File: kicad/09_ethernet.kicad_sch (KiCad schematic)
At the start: 0 parts

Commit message: Schematic complete: ethernet, emmc and adc sheets
- 09 ethernet: KSZ9031RNX with the Agilex 5 values and straps, RGMII 22R series,
  ferrite-fed analog rails, magjack J9, jack LED via 74LVC1G06
- 10 emmc: KIOXIA THGAMVG7T13BAIL, 47k pulls, CLK 10R, VCC 3V3 / VCCQ 1V8
- 13 adc: Agilex 3 card front end (SN74LV4051A, OPA365, 33R + 680p C0G,
  ADS7056 with DVDD 1V8), rail monitors on the mux
- attach/series_r/pull_r sheet helpers; STATUS.md updated

ERC: only the two known notes; all 92 pin-plan signals reach their loads.

Co-Authored-By: Claude Opus 5.5 <noreply@anthropic.com>
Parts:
- added C901, C921, C922, C924, C931, C932, C933, C934, C935, C936, C941, C942, C943, C950, C951: 100n, Capacitor_SMD:C_0402_1005Metric, symbol ti135_card:C
- added C910, C911: 27p, Capacitor_SMD:C_0402_1005Metric, symbol ti135_card:C
- added C920, C923: 22u, Capacitor_SMD:C_0805_2012Metric, symbol ti135_card:C
- added C930: 10u, Capacitor_SMD:C_0805_2012Metric, symbol ti135_card:C
- added C940: 4u7, Capacitor_SMD:C_0402_1005Metric, symbol ti135_card:C
- added FB901, FB902: BLM15PX121SN1D, Inductor_SMD:L_0402_1005Metric, symbol ti135_card:FerriteBead_Small
- added J9: RB1-125B8G1A, Connector_RJ:RJ45_UDE_RB1-125B8G1A, symbol ti135_card:RJ45_RB1-125B8G1A
- added R901, R902, R903, R904, R905, R906, R907, R908, R909, R910, R911, R912: 22R, Resistor_SMD:R_0402_1005Metric, symbol ti135_card:R
- added R920, R921, R922, R923, R924, R925, R926, R927: 4k7, Resistor_SMD:R_0402_1005Metric, symbol ti135_card:R
- added R928, R929: 1k, Resistor_SMD:R_0402_1005Metric, symbol ti135_card:R
- added R930: 10k, Resistor_SMD:R_0402_1005Metric, symbol ti135_card:R
- added R931: 12.1k 1%, Resistor_SMD:R_0402_1005Metric, symbol ti135_card:R
- added R950: 330R, Resistor_SMD:R_0402_1005Metric, symbol ti135_card:R
- added U901: KSZ9031RNXCA, Package_DFN_QFN:QFN-48-1EP_7x7mm_P0.5mm_EP5.15x5.15mm, symbol ti135_card:KSZ9031RNXCA
- added U902: 74LVC1G06GW, Package_TO_SOT_SMD:SOT-353_SC-70-5, symbol ti135_card:74LVC1G06
- added Y901: 25MHz, Crystal:Crystal_SMD_3225-4Pin_3.2x2.5mm, symbol ti135_card:Crystal_GND24
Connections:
- new net 1V2: C930.1, C931.1, C932.1, C933.1, C934.1, C935.1, C936.1, FB902.1, U901.14 (DVDDL), U901.18 (DVDDL), U901.23 (DVDDL), U901.26 (DVDDL), U901.30 (DVDDL), U901.39 (DVDDL), U901.4 (AVDDL), U901.9 (AVDDL)
- new net 1V8: C940.1, C941.1, C942.1, C943.1, C951.1, R920.1, R921.1, R922.1, R923.1, R924.1, R925.1, R926.1, R927.1, U901.16 (DVDDH), U901.34 (DVDDH), U901.40 (DVDDH), U902.5 (VCC)
- new net 3V3: FB901.1, R950.1
- new net GND: C901.2, C910.2, C911.2, C920.2, C921.2, C922.2, C923.2, C924.2, C930.2, C931.2, C932.2, C933.2, C934.2, C935.2, C936.2, C940.2, C941.2, C942.2, C943.2, C950.2, C951.2, J9.R10 (GND), J9.SH, R928.2, R929.2, R930.2, R931.2, U901.29 (VSS), U901.49 (PAD_GND), U902.3 (GND), Y901.2 (G), Y901.4 (G)
- new net eth_ct: C950.1, J9.R1 (CT)
- new net eth_int_n: R927.2, U901.38 (INT_N/PME_N2)
- new net eth_led_a: J9.L3, R950.2
- new net eth_led_k: J9.L4, U902.4
- new net eth_mdc: R926.2, U901.36 (MDC)
- new net eth_mdi_a_N: J9.R3 (TD1-), U901.3 (TXRXM_A)
- new net eth_mdi_a_P: J9.R2 (TD1+), U901.2 (TXRXP_A)
- new net eth_mdi_b_N: J9.R5 (TD2-), U901.6 (TXRXM_B)
- new net eth_mdi_b_P: J9.R4 (TD2+), U901.5 (TXRXP_B)
- new net eth_mdi_c_N: J9.R7 (TD3-), U901.8 (TXRXM_C)
- new net eth_mdi_c_P: J9.R6 (TD3+), U901.7 (TXRXP_C)
- new net eth_mdi_d_N: J9.R9 (TD4-), U901.11 (TXRXM_D)
- new net eth_mdi_d_P: J9.R8 (TD4+), U901.10 (TXRXP_D)
- new net eth_mdio: R925.2, U901.37 (MDIO)
- new net eth_rst_n: C901.1, R930.1, U901.42 (RESET_N)
- new net phy_avddh: C920.1, C921.1, C922.1, FB901.2, U901.1 (AVDDH), U901.12 (AVDDH)
- new net phy_avddl_pll: C923.1, C924.1, FB902.2, U901.44 (AVDDL_PLL)
- new net phy_iset: R931.1, U901.48 (ISET)
- new net phy_led1: R929.1, U901.17 (LED1/PHAD0/PME_N1), U902.2
- new net phy_led2: R928.1, U901.15 (LED2/PHYAD1)
- new net phy_led_mode: R924.2, U901.41 (CLK125_NDO/LED_MODE)
- new net phy_rx_ctl: R908.2, U901.33 (RX_DV/CLK125_EN)
- new net phy_rxc: R907.2, U901.35 (RX_CLK/PHYAD2)
- new net phy_rxd0: R909.2, U901.32 (RXD0/MODE0)
- new net phy_rxd1: R910.2, U901.31 (RXD1/MODE1)
- new net phy_rxd2: R911.2, U901.28 (RXD2/MODE2)
- new net phy_rxd3: R912.2, U901.27 (RXD3/MODE3)
- new net phy_tx_ctl: R902.2, U901.25 (TX_EN)
- new net phy_txc: R901.2, U901.24 (GTX_CLK)
- new net phy_txd0: R903.2, U901.19 (TXD0)
- new net phy_txd1: R904.2, U901.20 (TXD1)
- new net phy_txd2: R905.2, U901.21 (TXD2)
- new net phy_txd3: R906.2, U901.22 (TXD3)
- new net phy_xi: C910.1, U901.46 (XI), Y901.1
- new net phy_xo: C911.1, U901.45 (XO), Y901.3
- new net rgmii_rx_ctl: R908.1
- new net rgmii_rxc: R907.1
- new net rgmii_rxd0: R909.1, R920.2
- new net rgmii_rxd1: R910.1, R921.2
- new net rgmii_rxd2: R911.1, R922.2
- new net rgmii_rxd3: R912.1, R923.2
- new net rgmii_tx_ctl: R902.1
- new net rgmii_txc: R901.1
- new net rgmii_txd0: R903.1
- new net rgmii_txd1: R904.1
- new net rgmii_txd2: R905.1
- new net rgmii_txd3: R906.1
- no-connect marks 0 -> 5
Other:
- note added: "1V2 DVDDL/AVDDL (8 pins): 10u + 6 x 100n"
- note added: "1V8 DVDDH (3 pins): 4u7 + 3 x 100n"
- note added: "25 MHz crystal 3225, 27 p load (Agilex card values); place at the PHY"
- note added: "AVDDH (3V3) and AVDDL_PLL (1V2) through ferrites (Agilex FB1/FB2)"
- note added: "Jack LED: LED1 (1.8 V, active high with its PHYAD0 pull-down) -> U902 open-drain inverter -> LED cathode; anode via R950 to 3V3. Verify LED1 polarity at bring-up."
- note added: "KSZ9031RNX gigabit PHY, RGMII at 1.8 V to bank 4B. Values and straps from the Agilex 5 card (address 0, RGMII mode, single-LED mode). J9 = UDE RB1-125B8G1A magjack, placed per MECHANICAL.md."
- note added: "RGMII series 22 R: TX at the FPGA, RX at the PHY (source side)"
- note added: "Straps / pulls (1V8): MODE0..3 = 1 (RGMII), LED_MODE = 1 (single LED), PHYAD = 0, MDIO/MDC/INT pull-ups, RESET_N pull-down (PHY held in reset until the FPGA drives it)."

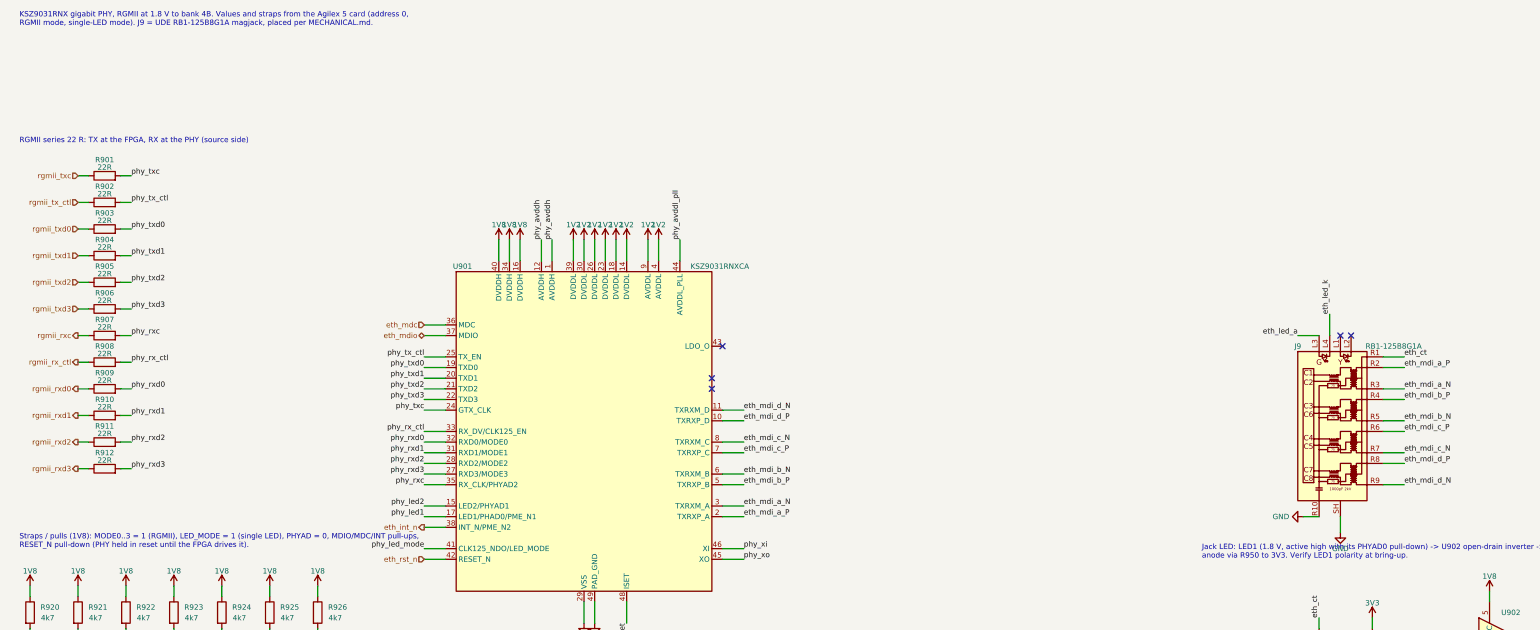
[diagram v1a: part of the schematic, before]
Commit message: PCB setup: board outline, fixed connectors, stack-up and rules; HR911130A magjack
- J9 magjack changed to HanRun HR911130A (C54408, 9124 orderable; RB1 had 0):
  generated footprint from the HanRun drawing, symbol, ethernet sheet updated,
  placed with the Ti60 jack's front face and centreline (MECHANICAL.md)
- tools/make_board.py: board from the netlist, outline, aux origin = Ti60
  origin, J3/J6 bottom sockets and J9 checked against MECHANICAL.md pads,
  U501 rotated 180 deg, U801 north, rest staged by sheet
- tools/board_setup.py: Agilex JLC08161H-3313 stack-up, LPDDR4/RGMII/power
  net classes, DRC rules (U501/U801), J3 edge exception
- DRC: parity 0, no shorts; only unrouted nets and edge silk warnings

Co-Authored-By: Claude Opus 5.5 <noreply@anthropic.com>
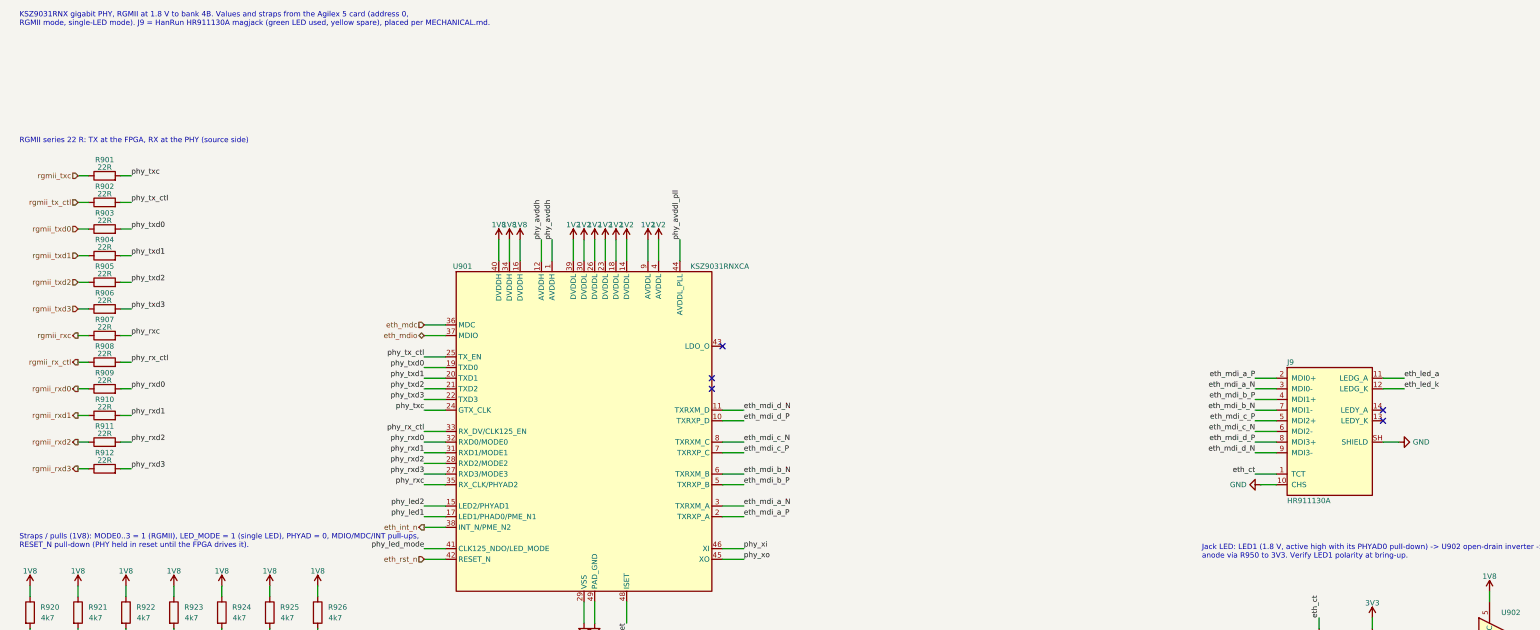
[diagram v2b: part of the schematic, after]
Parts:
- J9: value RB1-125B8G1A -> HR911130A; footprint Connector_RJ:RJ45_UDE_RB1-125B8G1A -> ti135_card:RJ45_Hanrun_HR911130A_Horizontal; symbol ti135_card:RJ45_RB1-125B8G1A -> ti135_card:HR911130A; LCSC C363353 -> C54408
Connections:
- net GND: now also J9.10 (CHS); no longer J9.R10 (GND)
- net eth_ct: now also J9.1 (TCT); no longer J9.R1 (CT)
- net eth_led_a: now also J9.11 (LEDG_A); no longer J9.L3
- net eth_led_k: now also J9.12 (LEDG_K); no longer J9.L4
- net eth_mdi_a_N: now also J9.3 (MDI0-); no longer J9.R3 (TD1-)
- net eth_mdi_a_P: now also J9.2 (MDI0+); no longer J9.R2 (TD1+)
- net eth_mdi_b_N: now also J9.7 (MDI1-); no longer J9.R5 (TD2-)
- net eth_mdi_b_P: now also J9.4 (MDI1+); no longer J9.R4 (TD2+)
- net eth_mdi_c_N: now also J9.6 (MDI2-); no longer J9.R7 (TD3-)
- net eth_mdi_c_P: now also J9.5 (MDI2+); no longer J9.R6 (TD3+)
- net eth_mdi_d_N: now also J9.9 (MDI3-); no longer J9.R9 (TD4-)
- net eth_mdi_d_P: now also J9.8 (MDI3+); no longer J9.R8 (TD4+)
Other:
- note added: "KSZ9031RNX gigabit PHY, RGMII at 1.8 V to bank 4B. Values and straps from the Agilex 5 card (address 0, RGMII mode, single-LED mode). J9 = HanRun HR911130A magjack (green LED used, yellow spare), placed per MECHANICAL.md."
- note removed: "KSZ9031RNX gigabit PHY, RGMII at 1.8 V to bank 4B. Values and straps from the Agilex 5 card (address 0, RGMII mode, single-LED mode). J9 = UDE RB1-125B8G1A magjack, placed per MECHANICAL.md."
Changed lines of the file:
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@@
 		(comment 1 "Efinix Ti135N484I3 control card for the AC lab PSU baseboard")
 	)
-	(text "KSZ9031RNX gigabit PHY, RGMII at 1.8 V to bank 4B. Values and straps from the Agilex 5 card (address 0,\nRGMII mode, single-LED mode). J9 = UDE RB1-125B8G1A magjack, placed per MECHANICAL.md."
+	(text "KSZ9031RNX gigabit PHY, RGMII at 1.8 V to bank 4B. Values and straps from the Agilex 5 card (address 0,\nRGMII mode, single-LED mode). J9 = HanRun HR911130A magjack (green LED used, yellow spare), placed per MECHANICAL.md."
 		(exclude_from_sim no)
 		(at 17.78 17.78 0)
@@
 	)
 	(symbol
-		(lib_id "ti135_card:RJ45_RB1-125B8G1A")
+		(lib_id "ti135_card:HR911130A")
 		(at 330.2 114.3 0)
 		(unit 1)
@@
 		(dnp no)
 		(property "Reference" "J9"
-			(at 322.58 93.98 0)
+			(at 320.04 97.79 0)
 			(effects
 				(font
 					(size 1.27 1.27)
 				)
+				(justify left)
 			)
 		)
-		(property "Value" "RB1-125B8G1A"
-			(at 345.44 93.98 0)
+		(property "Value" "HR911130A"
+			(at 320.04 130.81 0)
 			(effects
 				(font
 					(size 1.27 1.27)
 				)
+				(justify left)
 			)
 		)
-		(property "Footprint" "Connector_RJ:RJ45_UDE_RB1-125B8G1A"
-			(at 331.47 111.76 0)
+		(property "Footprint" "ti135_card:RJ45_Hanrun_HR911130A_Horizontal"
+			(at 330.2 114.3 0)
 			(effects
 				(font
@@
 			)
 		)
-		(property "Datasheet" ""
-			(at 324.104 113.157 0)
+		(property "Datasheet" "https://datasheet.lcsc.com/datasheet/pdf/d9b1e130e54a44fe9872ced55aa393e4.pdf"
+			(at 330.2 114.3 0)
 			(effects
 				(font
 					(size 1.27 1.27)
 				)
-				(justify left top)
 				(hide yes)
 			)
 		)
-		(property "Description" "LAN Transformer Jack, RJ45, 10/100/1000 BaseT"
+		(property "Description" "HanRun RJ45 with 10/100/1000Base-T magnetics, green (11 A / 12 K) and yellow (14 A / 13 K) LEDs. TCT = chip-side centre taps, CHS = 75 R / 1000 p Bob Smith common (LCSC C54408)"
 			(at 330.2 114.3 0)
 			(effects
@@
 			)
 		)
-		(property "LCSC" "C363353"
+		(property "LCSC" "C54408"
 			(at 330.2 114.3 0)
 			(effects
@@
 			)
 		)
-		(pin "R10"
+		(pin "2"
 		)
-		(pin "L1"
+		(pin "3"
 		)
-		(pin "L2"
+		(pin "4"
 		)
-		(pin "L3"
+		(pin "7"
 		)
-		(pin "L4"
+		(pin "5"
 		)
-		(pin "R1"
+		(pin "6"
 		)
-		(pin "R2"
+		(pin "8"
 		)
-		(pin "R3"
+		(pin "9"
 		)
-		(pin "R4"
+		(pin "1"
 		)
-		(pin "R5"
+		(pin "10"
 		)
-		(pin "R6"
+		(pin "11"
 		)
-		(pin "R7"
+		(pin "12"
 		)
-		(pin "R8"
+		(pin "14"
 		)
-		(pin "R9"
+		(pin "13"
 		)
 		(pin "SH"
@@
 	(wire
 		(pts
-			(xy 342.9 99.06) (xy 347.98 99.06)
+			(xy 317.5 101.6) (xy 312.42 101.6)
 		)
 		(stroke
@@
 	)
 	(label "eth_mdi_a_P"
-		(at 347.98 99.06 0)
+		(at 312.42 101.6 180)
 		(effects
 			(font
 				(size 1.27 1.27)
 			)
-			(justify left bottom)
+			(justify right bottom)
 		)
 	)
 	(wire
 		(pts
-			(xy 342.9 104.14) (xy 347.98 104.14)
+			(xy 317.5 104.14) (xy 312.42 104.14)
 		)
 		(stroke
@@
 	)
 	(label "eth_mdi_a_N"
-		(at 347.98 104.14 0)
+		(at 312.42 104.14 180)
 		(effects
 			(font
 				(size 1.27 1.27)
 			)
-			(justify left bottom)
+			(justify right bottom)
 		)
 	)
 	(wire
 		(pts
-			(xy 342.9 106.68) (xy 347.98 106.68)
+			(xy 317.5 106.68) (xy 312.42 106.68)
 		)
 		(stroke
@@
 	)
 	(label "eth_mdi_b_P"
-		(at 347.98 106.68 0)
+		(at 312.42 106.68 180)
 		(effects
 			(font
 				(size 1.27 1.27)
 			)
-			(justify left bottom)
+			(justify right bottom)
 		)
 	)
 	(wire
 		(pts
-			(xy 342.9 111.76) (xy 347.98 111.76)
+			(xy 317.5 109.22) (xy 312.42 109.22)
 		)
 		(stroke
@@
 	)
 	(label "eth_mdi_b_N"
-		(at 347.98 111.76 0)
+		(at 312.42 109.22 180)
 		(effects
 			(font
 				(size 1.27 1.27)
 			)
-			(justify left bottom)
+			(justify right bottom)
 		)
 	)
 	(wire
 		(pts
-			(xy 342.9 114.3) (xy 347.98 114.3)
+			(xy 317.5 111.76) (xy 312.42 111.76)
 		)
 		(stroke
@@
 	)
 	(label "eth_mdi_c_P"
-		(at 347.98 114.3 0)
+		(at 312.42 111.76 180)
 		(effects
 			(font
 				(size 1.27 1.27)
 			)
-			(justify left bottom)
+			(justify right bottom)
 		)
 	)
 	(wire
 		(pts
-			(xy 342.9 119.38) (xy 347.98 119.38)
+			(xy 317.5 114.3) (xy 312.42 114.3)
 		)
 		(stroke
@@
 	)
 	(label "eth_mdi_c_N"
-		(at 347.98 119.38 0)
+		(at 312.42 114.3 180)
 		(effects
 			(font
 				(size 1.27 1.27)
 			)
-			(justify left bottom)
+			(justify right bottom)
 		)
 	)
 	(wire
 		(pts
-			(xy 342.9 121.92) (xy 347.98 121.92)
+			(xy 317.5 116.84) (xy 312.42 116.84)
 		)
 		(stroke
@@
 	)
 	(label "eth_mdi_d_P"
-		(at 347.98 121.92 0)
+		(at 312.42 116.84 180)
 		(effects
 			(font
 				(size 1.27 1.27)
 			)
-			(justify left bottom)
+			(justify right bottom)
 		)
 	)
 	(wire
 		(pts
-			(xy 342.9 127) (xy 347.98 127)
+			(xy 317.5 119.38) (xy 312.42 119.38)
 		)
 		(stroke
@@
 	)
 	(label "eth_mdi_d_N"
-		(at 347.98 127 0)
+		(at 312.42 119.38 180)
 		(effects
 			(font
 				(size 1.27 1.27)
 			)
-			(justify left bottom)
+			(justify right bottom)
 		)
 	)
 	(wire
 		(pts
-			(xy 342.9 96.52) (xy 347.98 96.52)
+			(xy 317.5 124.46) (xy 312.42 124.46)
 		)
 		(stroke
@@
 	)
 	(label "eth_ct"
-		(at 347.98 96.52 0)
+		(at 312.42 124.46 180)
 		(effects
 			(font
 				(size 1.27 1.27)
 			)
-			(justify left bottom)
+			(justify right bottom)
 		)
 	)
 	(wire
 		(pts
-			(xy 327.66 134.62) (xy 323.85 134.62)
+			(xy 317.5 127) (xy 313.69 127)
 		)
 		(stroke
@@
 	(symbol
 		(lib_id "ti135_card:GND")
-		(at 323.85 134.62 270)
+		(at 313.69 127 270)
 		(unit 1)
 		(exclude_from_sim no)
@@
 		(dnp no)
 		(property "Reference" "#PWR044"
-			(at 317.5 134.62 0)
+			(at 307.34 127 0)
 			(effects
 				(font
@@
 		)
 		(property "Value" "GND"
-			(at 320.55 134.62 270)
+			(at 310.39 127 270)
 			(effects
 				(font
@@
 		)
 		(property "Footprint" ""
-			(at 323.85 134.62 0)
+			(at 313.69 127 0)
 			(effects
 				(font
@@
 		)
 		(property "Datasheet" ""
-			(at 323.85 134.62 0)
+			(at 313.69 127 0)
 			(effects
 				(font
@@
 		)
 		(property "Description" "Power symbol for net \"GND\" (IPC net name)"
-			(at 323.85 134.62 0)
+			(at 313.69 127 0)
 			(effects
 				(font
@@
 	(wire
 		(pts
-			(xy 332.74 134.62) (xy 332.74 138.43)
+			(xy 342.9 116.84) (xy 346.71 116.84)
 		)
 		(stroke
@@
 	(symbol
 		(lib_id "ti135_card:GND")
-		(at 332.74 138.43 0)
+		(at 346.71 116.84 90)
 		(unit 1)
 		(exclude_from_sim no)
@@
 		(dnp no)
 		(property "Reference" "#PWR045"
-			(at 332.74 144.78 0)
+			(at 353.06 116.84 0)
 			(effects
 				(font
@@
 		)
 		(property "Value" "GND"
-			(at 332.74 142.24 0)
+			(at 350.01 116.84 90)
 			(effects
 				(font
 					(size 1.27 1.27)
 				)
+				(justify right)
 			)
 		)
 		(property "Footprint" ""
-			(at 332.74 138.43 0)
+			(at 346.71 116.84 0)
 			(effects
 				(font
@@
 		)
 		(property "Datasheet" ""
-			(at 332.74 138.43 0)
+			(at 346.71 116.84 0)
 			(effects
 				(font
@@
 		)
 		(property "Description" "Power symbol for net \"GND\" (IPC net name)"
-			(at 332.74 138.43 0)
+			(at 346.71 116.84 0)
 			(effects
 				(font
@@
 		)
 	)
-	(no_connect
-		(at 332.74 91.44)
-	)
-	(no_connect
-		(at 335.28 91.44)
-	)
 	(wire
 		(pts
-			(xy 327.66 91.44) (xy 322.58 91.44)
+			(xy 342.9 101.6) (xy 347.98 101.6)
 		)
 		(stroke
@@
 	)
 	(label "eth_led_a"
-		(at 322.58 91.44 180)
+		(at 347.98 101.6 0)
 		(effects
 			(font
 				(size 1.27 1.27)
 			)
-			(justify right bottom)
+			(justify left bottom)
 		)
 	)
 	(wire
 		(pts
-			(xy 330.2 91.44) (xy 330.2 86.36)
+			(xy 342.9 104.14) (xy 347.98 104.14)
 		)
 		(stroke
@@
 	)
 	(label "eth_led_k"
-		(at 330.2 86.36 90)
+		(at 347.98 104.14 0)
 		(effects
 			(font
@@
 		)
 	)
+	(no_connect
+		(at 342.9 109.22)
+	)
+	(no_connect
+		(at 342.9 111.76)
+	)
 	(symbol
